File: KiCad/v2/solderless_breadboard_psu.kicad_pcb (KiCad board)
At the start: 4 copper layers, 53 x 51 mm, 78 parts, among them IC201 TPS63000DRCR, IC202 TPS63000DRCR, IC301 CP2102N-A02-GQFN24R, J201 Conn_01x02_Pin, J202 Conn_01x03_Pin, J203 Conn_02x03_Odd_Even, J204 Conn_01x03_Pin, J205 Conn_02x03_Odd_Even, J301 Conn_01x09_Pin, J302 Conn_01x09_Pin, J303 Conn_01x06_Pin, J304 USB_C_Receptacle_USB2.0_16P, J305 Conn_01x03_Pin, U301 USBLC6-2SC6

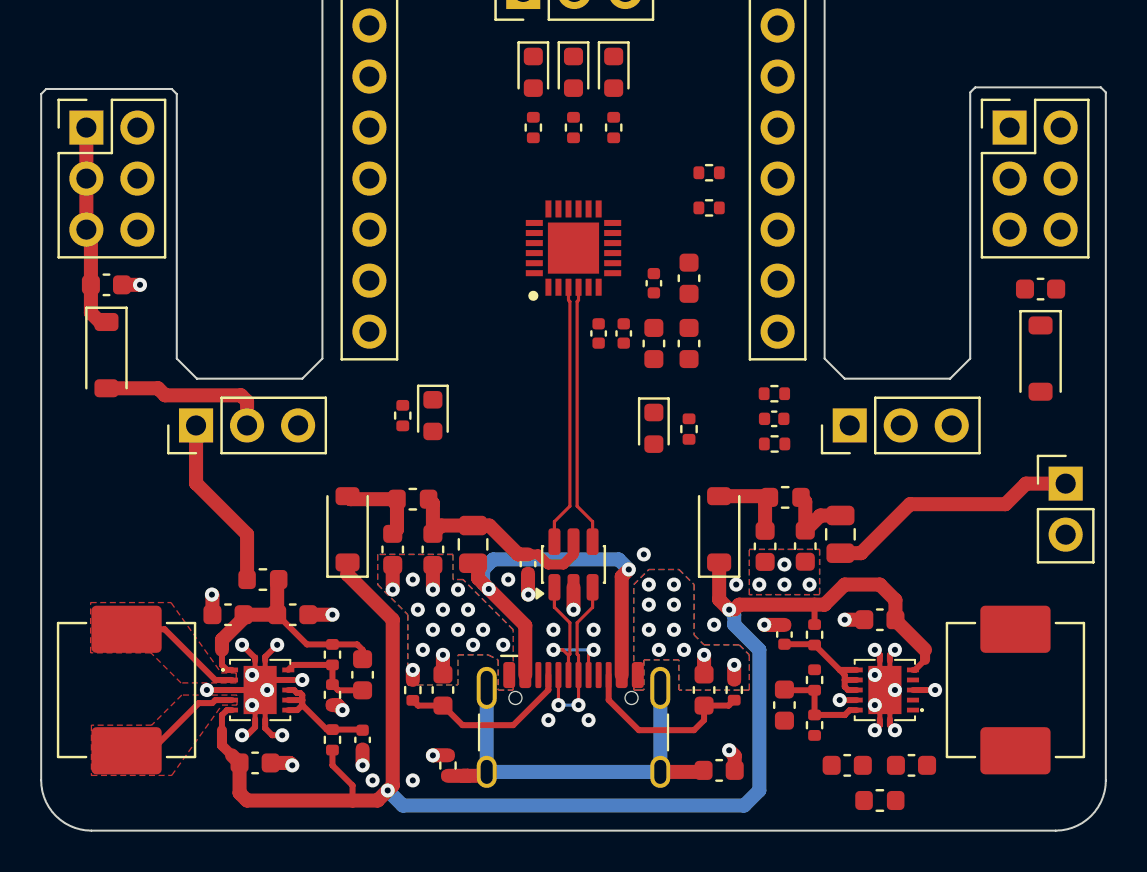
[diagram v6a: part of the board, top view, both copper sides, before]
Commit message: power signals routing
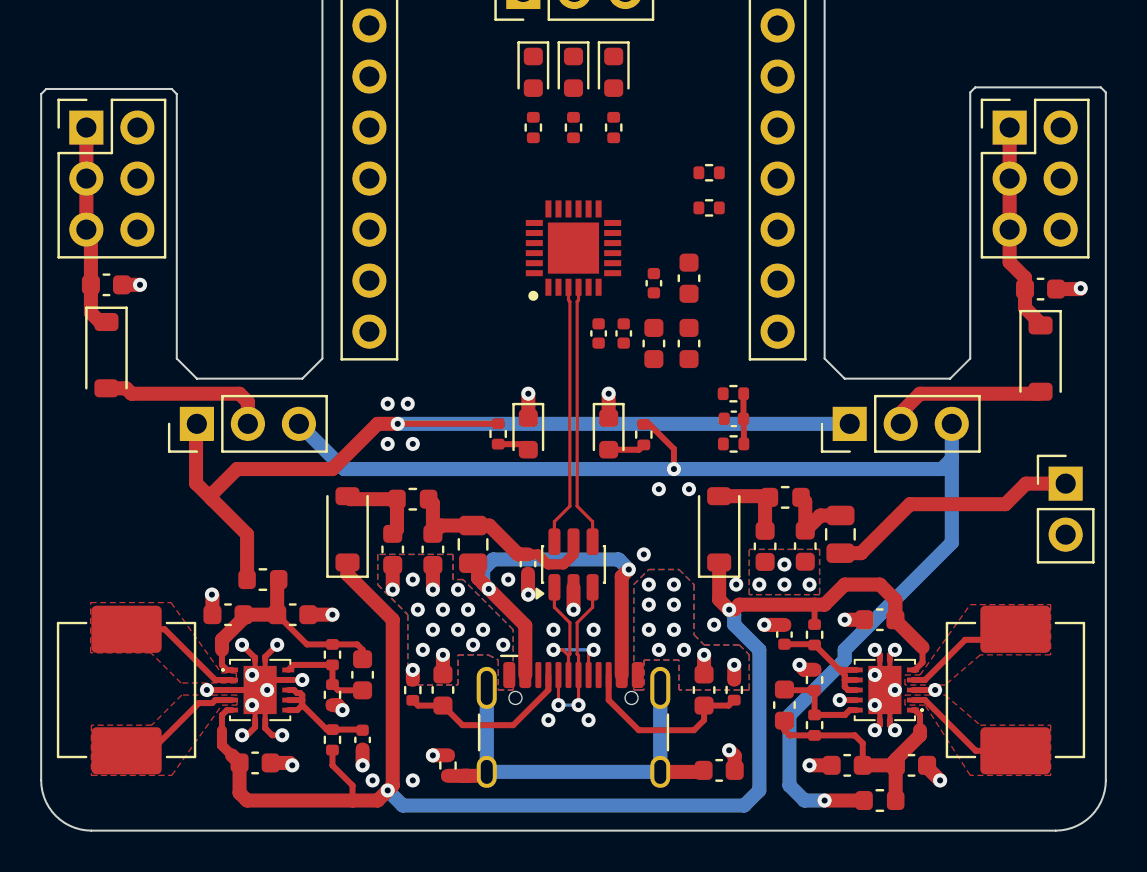
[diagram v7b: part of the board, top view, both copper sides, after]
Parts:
- moved D202 4.84 mm to (74.2, 81.2)
- moved R201 4.84 mm to (72.8, 81.2)
- moved D204 2.27 mm to (78.2, 81.2)
- moved R205 2.27 mm to (80.0, 81.3), turned to 90 degrees
- moved R301 2.04 mm to (84.5, 81.8), turned to 0 degrees
- moved R302 2.04 mm to (84.5, 79.2), turned to 180 degrees
- moved C303 2.01 mm to (84.5, 80.5), turned to 180 degrees
- moved J202 0.09 mm to (57.8, 80.8)
- moved J204 0.08 mm to (90.2, 80.8)
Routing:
- net +3V3: track 0.00 -> 62.0 mm, vias 0 -> 2
- net +5V: track 8.72 -> 47.3 mm, vias 0 -> 1
- net /[2] Power/3V3_OUT: track 0.00 -> 12.6 mm
- net VCC_R: track 0.00 -> 10.5 mm
- net Net-(D206-A): track 0.00 -> 7.94 mm
- net GND: track 31.6 -> 38.2 mm, vias 69 -> 81
- net /[2] Power/3V3_L2: track 0.00 -> 6.15 mm
- net /[2] Power/3V3_L1: track 0.00 -> 6.15 mm
- net /[3] USB 2 UART/VBUS: track 0.00 -> 2.50 mm
- net Net-(D204-A): track 0.00 -> 1.85 mm
- net Net-(D202-A): track 0.00 -> 1.61 mm
- added copper zone on F.Cu, net /[2] Power/3V3_L1
- added copper zone on F.Cu, net /[2] Power/3V3_L2

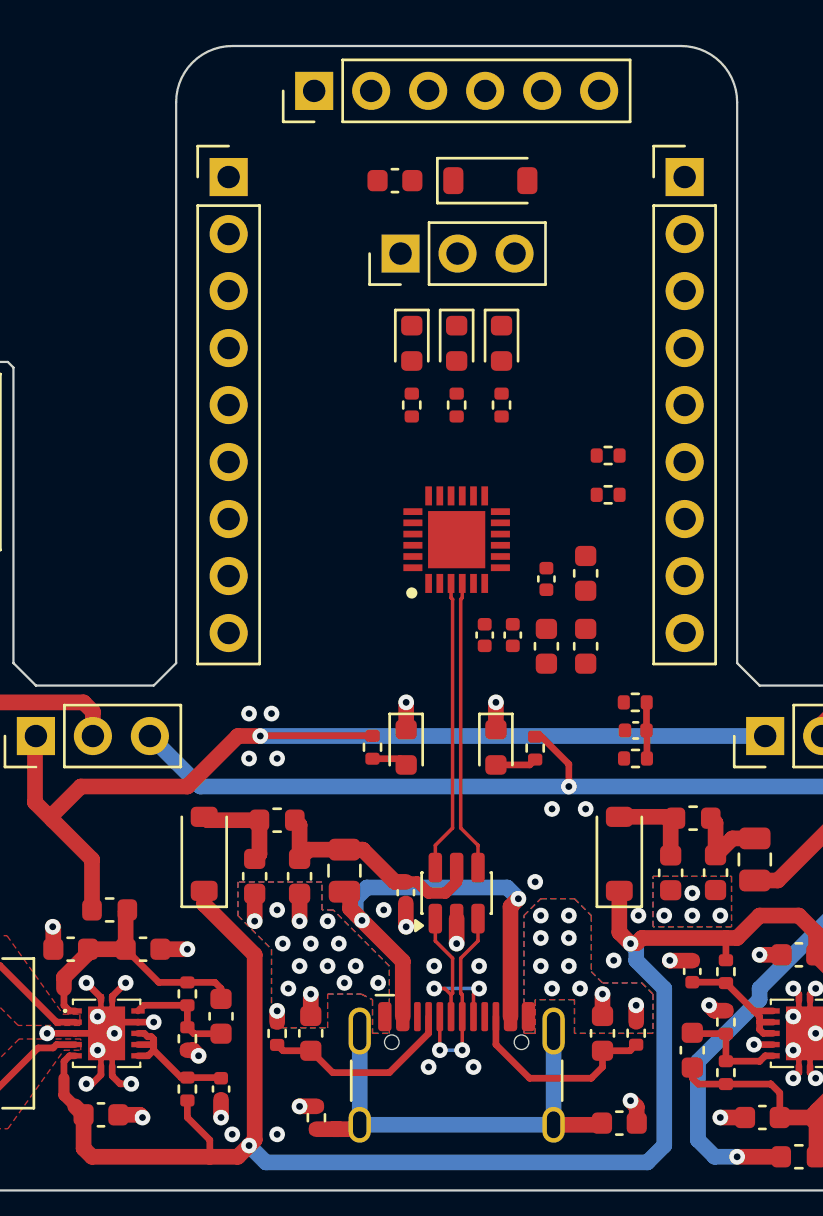
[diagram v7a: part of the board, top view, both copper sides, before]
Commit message: Signal routing
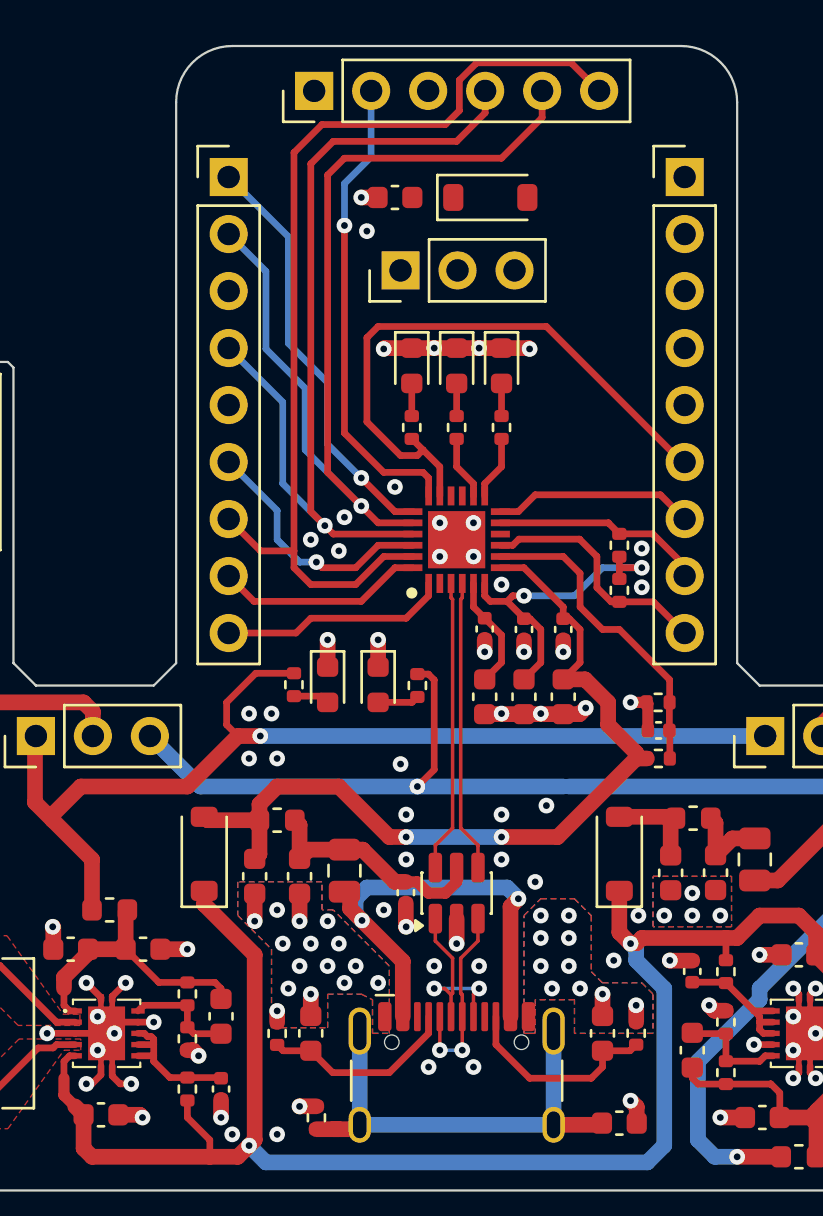
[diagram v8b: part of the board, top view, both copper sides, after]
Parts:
- moved D204 5.94 mm to (73.0, 78.5)
- moved R205 5.94 mm to (74.8, 78.5)
- moved C306 5.59 mm to (81.2, 79.0), turned to -90 degrees
- moved D202 4.47 mm to (70.8, 78.5)
- moved R201 4.47 mm to (69.2, 78.5)
- moved R303 4.29 mm to (83.8, 74.3), turned to -90 degrees
- moved R309 4.03 mm to (83.8, 72.2), turned to 90 degrees
- moved C302 3.55 mm to (79.5, 79.0)
- moved C305 3.55 mm to (77.8, 79.0)
- moved C307 2.37 mm to (81.2, 76.0), turned to -90 degrees
- moved R302 1.02 mm to (85.5, 79.2)
- moved C303 1.02 mm to (85.5, 80.5)
- moved R301 1.02 mm to (85.5, 81.8)
- moved D301 1.00 mm to (74.5, 64.2)
- moved D302 1.00 mm to (78.5, 64.2)
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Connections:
- J301 pad 6: /[3] USB 2 UART/WAKEUP -> /[3] USB 2 UART/SUSPEND
- J301 pad 7: /[3] USB 2 UART/RSTB -> /[3] USB 2 UART/RS485
- J301 pad 8: /[3] USB 2 UART/SUSPEND -> /[3] USB 2 UART/WAKEUP
- J301 pad 9: /[3] USB 2 UART/RS485 -> /[3] USB 2 UART/RSTB
- J302 pad 1: /[3] USB 2 UART/TXD -> /[3] USB 2 UART/RTS
- J302 pad 2: /[3] USB 2 UART/DTR -> /[3] USB 2 UART/RXD
- J302 pad 3: /[3] USB 2 UART/RTS -> GND
- J302 pad 4: GND -> /[3] USB 2 UART/TXD
- J302 pad 5: /[3] USB 2 UART/RXD -> GND
- J302 pad 6: /[3] USB 2 UART/RI -> /[3] USB 2 UART/DSR
- J302 pad 7: GND -> /[3] USB 2 UART/DTR
- J302 pad 8: /[3] USB 2 UART/DSR -> /[3] USB 2 UART/DCD
- J302 pad 9: /[3] USB 2 UART/DCD -> /[3] USB 2 UART/CLK
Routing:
- net /[3] USB 2 UART/DTR: track 0.00 -> 45.1 mm
- net /[3] USB 2 UART/RXD: track 0.00 -> 44.4 mm, vias 0 -> 1
- net /[3] USB 2 UART/TXD: track 0.00 -> 39.8 mm, vias 0 -> 1
- net VUSB_FILT: track 4.34 -> 38.0 mm, vias 0 -> 2
- net /[3] USB 2 UART/SUSPEND: track 0.00 -> 26.9 mm
- net /[3] USB 2 UART/CTS: track 0.00 -> 21.1 mm, vias 0 -> 1
- net UART_VDD: track 0.00 -> 19.9 mm, vias 0 -> 2
- net /[3] USB 2 UART/RTS: track 0.00 -> 18.8 mm, vias 0 -> 1
- net GND: track 38.2 -> 53.6 mm, vias 81 -> 109
- net /[3] USB 2 UART/VBUS: track 2.50 -> 14.2 mm
- net /[3] USB 2 UART/DSR: track 0.00 -> 11.3 mm, vias 0 -> 1
- net /[3] USB 2 UART/RSTB: track 0.00 -> 10.9 mm
- net /[3] USB 2 UART/CLK: track 0.00 -> 10.1 mm
- net /[3] USB 2 UART/WAKEUP: track 0.00 -> 9.47 mm
- net /[3] USB 2 UART/DCD: track 0.00 -> 9.30 mm
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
